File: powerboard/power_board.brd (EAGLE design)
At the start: 152.4 x 86.4 mm, 100 parts, among them Q1 IPP80P03P4L04AKSA1, U1 UWQ-12/20-T48NBS-C, U2 UWE-5/20-Q48NB-C, U3 UWE-3.3/30-Q48NB-C

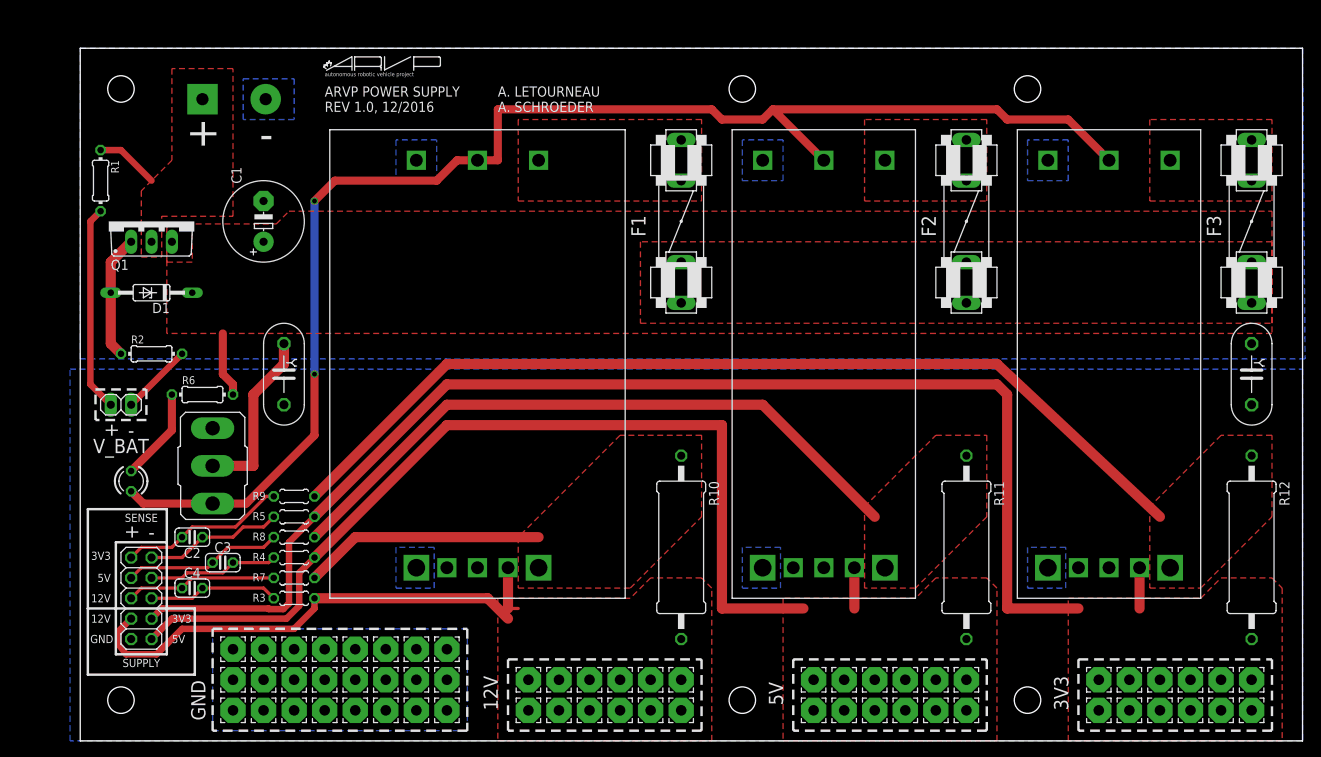
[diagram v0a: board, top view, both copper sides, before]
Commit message: Changed position of V_BAT current limiting resistor.
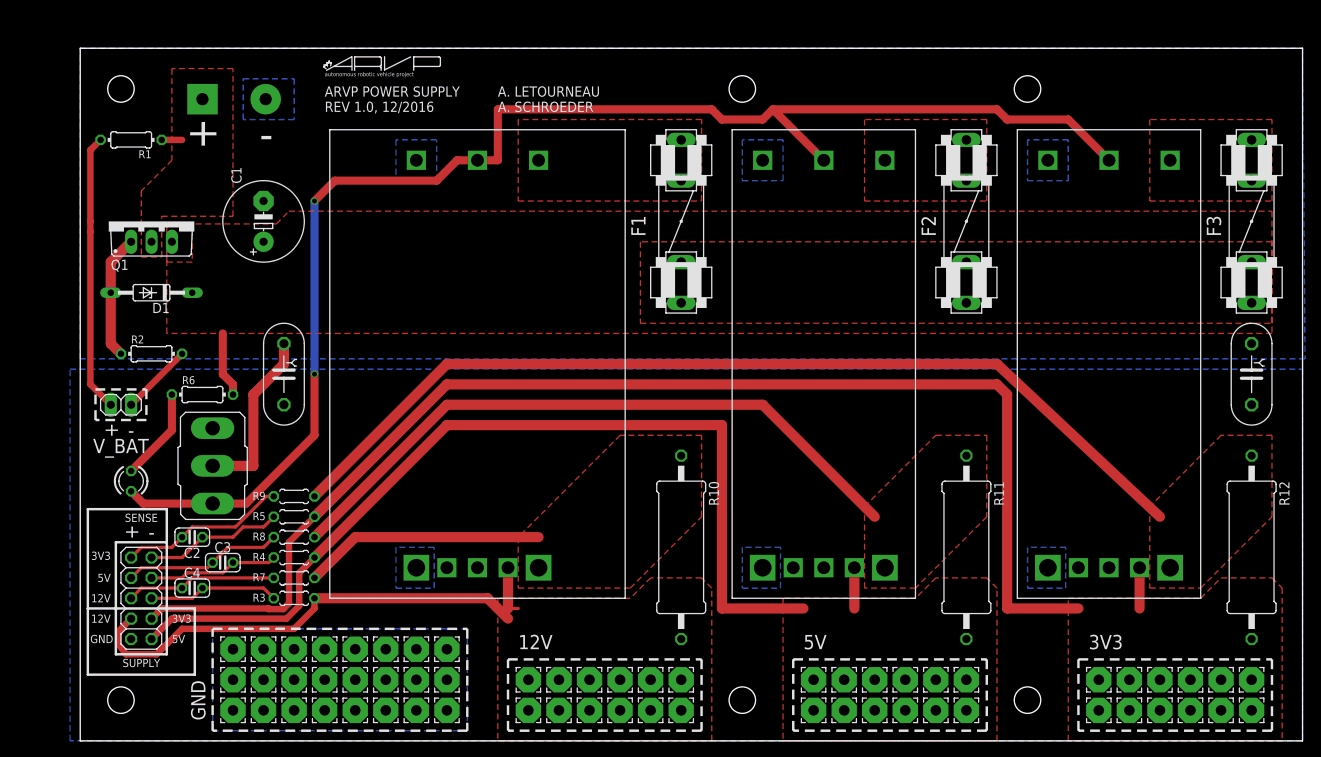
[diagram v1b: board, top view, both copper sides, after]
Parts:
- moved R1 6.35 mm to (35.6, 66.0), turned to 180 degrees
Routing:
- net N$2: track 25.7 -> 34.6 mm
- net VBAT+: track 7.93 -> 2.54 mm
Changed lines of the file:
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@@
 <setting verticaltext="up"/>
 </settings>
-<grid distance="1" unitdist="mm" unit="mm" style="lines" multiple="1" display="yes" altdistance="1" altunitdist="mm" altunit="mm"/>
+<grid distance="0.05" unitdist="inch" unit="inch" style="lines" multiple="1" display="yes" altdistance="0.0125" altunitdist="inch" altunit="inch"/>
 <layers>
 <layer number="1" name="Top" color="4" fill="1" visible="yes" active="yes"/>
@@
 <wire x1="106.68" y1="1.27" x2="106.68" y2="-7.62" width="0.3048" layer="25" style="longdash"/>
 <wire x1="106.68" y1="-7.62" x2="82.55" y2="-7.62" width="0.3048" layer="25" style="longdash"/>
-<text x="81.28" y="-5.08" size="1.778" layer="25" rot="R90">12V</text>
-<text x="116.84" y="-4.445" size="1.778" layer="25" rot="R90">5V</text>
-<text x="152.4" y="-5.08" size="1.778" layer="25" rot="R90">3V3</text>
+<text x="83.82" y="2.54" size="1.778" layer="25">12V</text>
+<text x="119.38" y="2.54" size="1.778" layer="25">5V</text>
+<text x="154.94" y="2.54" size="1.778" layer="25">3V3</text>
 <wire x1="118.11" y1="-7.62" x2="118.11" y2="1.27" width="0.3048" layer="25" style="longdash"/>
 <wire x1="118.11" y1="1.27" x2="142.24" y2="1.27" width="0.3048" layer="25" style="longdash"/>
@@
 </element>
 <element name="P$1" library="ARVP" package="AND_PWR" value="AND_PWR" x="44.45" y="71.12" rot="R90"/>
-<element name="R1" library="resistor" package="0204/7" value="1k" x="31.75" y="60.96" rot="R270"/>
+<element name="R1" library="resistor" package="0204/7" value="1k" x="35.56" y="66.04" rot="R180"/>
 </elements>
 <signals>
@@
 <contactref element="P$1" pad="PWR"/>
 <contactref element="R1" pad="1"/>
-<wire x1="31.75" y1="64.77" x2="34.29" y2="64.77" width="0.8128" layer="1"/>
-<wire x1="34.29" y1="64.77" x2="38.1" y2="60.96" width="0.8128" layer="1"/>
+<wire x1="39.37" y1="66.04" x2="41.91" y2="66.04" width="0.8128" layer="1"/>
 </signal>
 <signal name="N$4">
@@
 <contactref element="R1" pad="2"/>
 <contactref element="JP7" pad="1"/>
-<wire x1="31.75" y1="57.15" x2="30.48" y2="55.88" width="0.8128" layer="1"/>
-<wire x1="30.48" y1="55.88" x2="30.48" y2="35.56" width="0.8128" layer="1"/>
+<wire x1="30.48" y1="55.88" x2="30.48" y2="54.61" width="0.8128" layer="1"/>
+<wire x1="30.48" y1="54.61" x2="30.48" y2="35.56" width="0.8128" layer="1"/>
 <wire x1="30.48" y1="35.56" x2="33.02" y2="33.02" width="0.8128" layer="1"/>
+<wire x1="31.75" y1="66.04" x2="30.48" y2="64.77" width="0.8128" layer="1"/>
+<wire x1="30.48" y1="64.77" x2="30.48" y2="55.88" width="0.8128" layer="1"/>
 </signal>
 </signals>

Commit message: Removed toggle switch and added 2 position screw type terminal block.
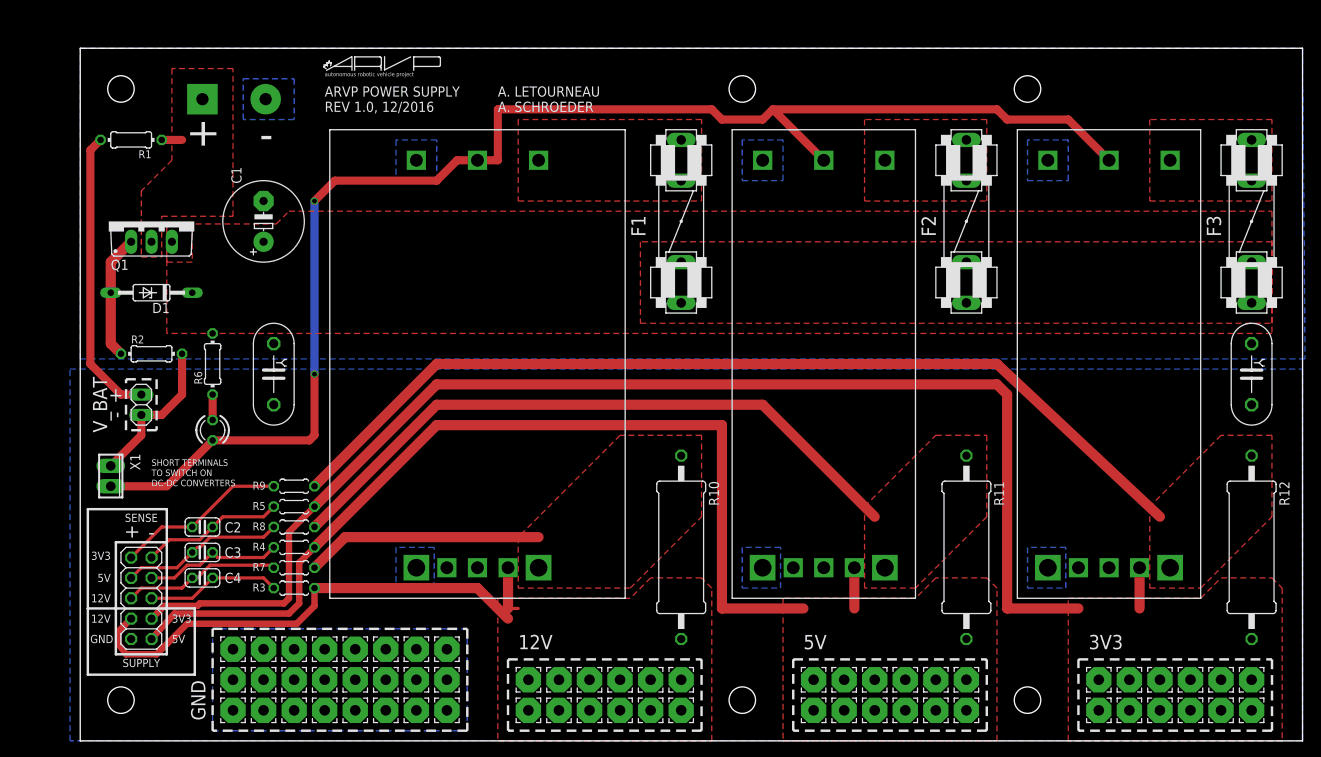
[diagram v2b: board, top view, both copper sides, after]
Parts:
- removed S1: (no value), switch:M9040P
- added X1: (no value), con-phoenix-254:2POL254
- moved LED1 12.0 mm to (45.7, 29.8)
- moved R6 4.02 mm to (45.7, 38.1), turned to 90 degrees
- moved C3 2.84 mm to (44.5, 14.6)
- moved JP7 2.54 mm to (36.8, 33.0), turned to 270 degrees
- moved C2 1.80 mm to (44.5, 17.8)
- moved C4 1.80 mm to (44.5, 11.4)
- moved R3 1.27 mm to (55.9, 10.2)
- moved R4 1.27 mm to (55.9, 15.2)
- moved R5 1.27 mm to (55.9, 20.3)
- moved R7 1.27 mm to (55.9, 12.7)
- moved R8 1.27 mm to (55.9, 17.8)
- moved R9 1.27 mm to (55.9, 22.9)
- moved CY1 1.27 mm to (53.3, 36.8)
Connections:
- net ON/OFF: now also X1.2; no longer S1.1
- net V-: now also X1.1; no longer S1.2
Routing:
- net V-: track 30.9 -> 19.1 mm
- net N$1: track 11.6 -> 3.18 mm
- net V+: track 8.15 -> 0.00 mm
- net N$2: track 34.6 -> 36.4 mm
- net 12V-SENSE: track 64.1 -> 65.7 mm
- net J5: track 16.3 -> 17.3 mm
- net ON/OFF: track 176.4 -> 177.4 mm
- net J4: track 18.8 -> 19.6 mm
- net 5V-SENSE: track 122.7 -> 123.3 mm
- net J8: track 20.9 -> 21.5 mm
- net J7: track 17.3 -> 17.9 mm
- net J3: track 16.3 -> 16.8 mm
- net 12V+SENSE: track 30.0 -> 29.5 mm
- net J6: track 19.9 -> 20.4 mm
- net 5V+SENSE: track 82.5 -> 81.9 mm
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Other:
- board text added: "DC-DC CONVERTERS"
- board text added: "SHORT TERMINALS"
- board text added: "TO SWITCH ON"

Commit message: Reduced length of board to 5.9 inches
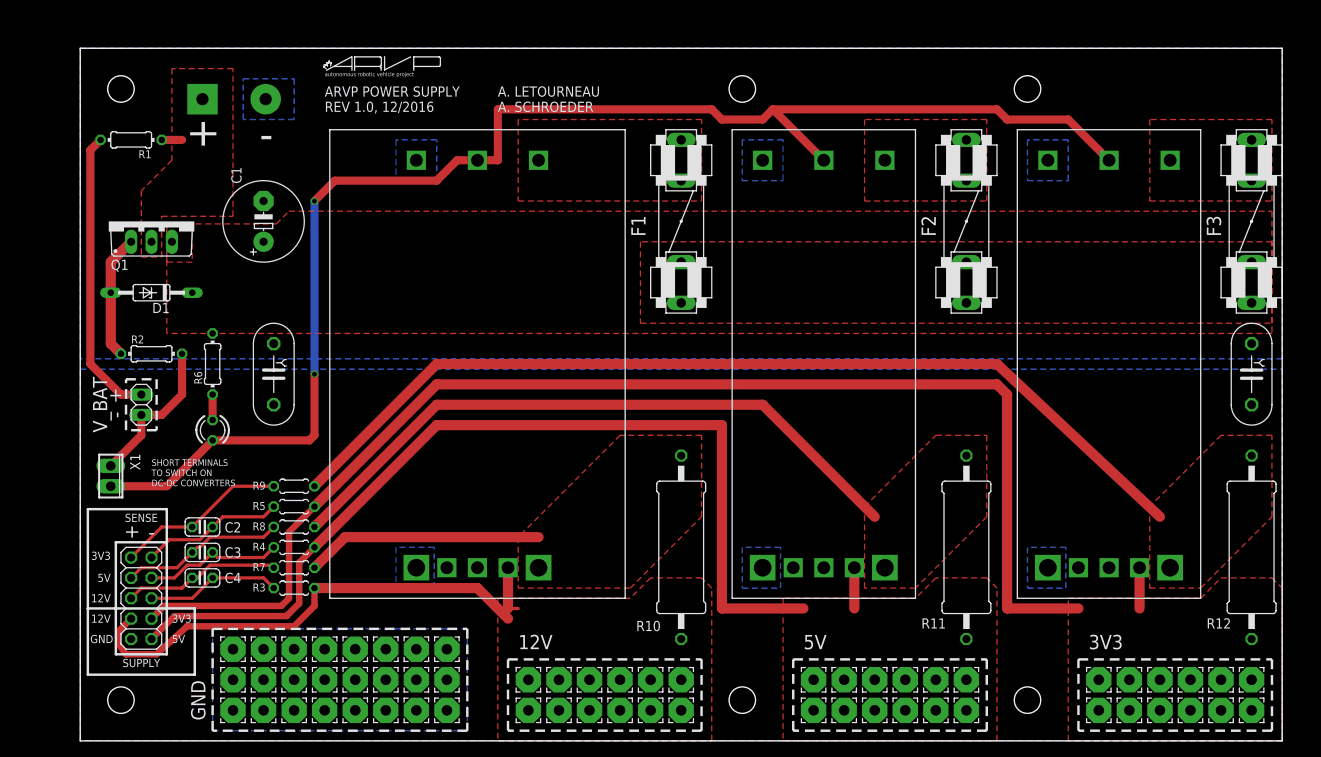
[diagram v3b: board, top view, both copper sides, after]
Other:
- board size 152.4 x 86.4 mm -> 149.9 x 86.4 mm
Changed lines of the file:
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@@
 <board>
 <plain>
-<wire x1="29.21" y1="-8.89" x2="181.61" y2="-8.89" width="0" layer="20"/>
-<wire x1="181.61" y1="-8.89" x2="181.61" y2="77.47" width="0" layer="20"/>
-<wire x1="181.61" y1="77.47" x2="29.21" y2="77.47" width="0" layer="20"/>
+<wire x1="29.21" y1="-8.89" x2="179.07" y2="-8.89" width="0" layer="20"/>
+<wire x1="179.07" y1="-8.89" x2="179.07" y2="77.47" width="0" layer="20"/>
+<wire x1="179.07" y1="77.47" x2="29.21" y2="77.47" width="0" layer="20"/>
 <wire x1="29.21" y1="77.47" x2="29.21" y2="-8.89" width="0" layer="20"/>
-<dimension x1="181.61" y1="-8.89" x2="181.61" y2="77.47" x3="193.04" y3="34.29" textsize="1.778" layer="20" unit="inch" precision="3" visible="yes"/>
-<dimension x1="181.61" y1="77.47" x2="29.21" y2="77.47" x3="105.41" y3="90.17" textsize="1.778" layer="20" unit="inch" precision="3" visible="yes"/>
+<dimension x1="179.07" y1="-8.89" x2="179.07" y2="77.47" x3="190.5" y3="34.29" textsize="1.778" layer="20" unit="inch" precision="3" visible="yes"/>
 <text x="33.02" y="6.35" size="1.016" layer="25" align="center-right">12V</text>
 <text x="40.64" y="3.81" size="1.016" layer="25" align="center-left">5V</text>
@@
 <text x="38.1" y="24.13" size="0.8128" layer="25">TO SWITCH ON</text>
 <text x="38.1" y="22.86" size="0.8128" layer="25">DC-DC CONVERTERS</text>
+<dimension x1="179.07" y1="77.47" x2="29.21" y2="77.47" x3="104.14" y3="91.44" textsize="1.778" layer="20" unit="inch" visible="yes"/>
 </plain>
 <attributes>
@@
 <attribute name="VALUE" x="171.069" y="40.767" size="1.27" layer="27" ratio="10" rot="R270"/>
 </element>
-<element name="R10" library="rcl" package="0617/22" value="0.004" x="104.14" y="15.24" rot="R270"/>
-<element name="R11" library="rcl" package="0617/22" value="0.004" x="139.7" y="15.24" rot="R270"/>
-<element name="R12" library="rcl" package="0617/22" value="0.004" x="175.26" y="15.24" rot="R270"/>
+<element name="R10" library="rcl" package="0617/22" value="0.004" x="104.14" y="15.24" smashed="yes" rot="R270">
+<attribute name="NAME" x="101.6" y="6.0706" size="1.27" layer="25" ratio="10" rot="R180"/>
+<attribute name="VALUE" x="103.5558" y="21.717" size="1.27" layer="27" ratio="10" rot="R270"/>
+</element>
+<element name="R11" library="rcl" package="0617/22" value="0.004" x="139.7" y="15.24" smashed="yes" rot="R270">
+<attribute name="NAME" x="137.16" y="6.3881" size="1.27" layer="25" ratio="10" rot="R180"/>
+<attribute name="VALUE" x="139.1158" y="21.717" size="1.27" layer="27" ratio="10" rot="R270"/>
+</element>
+<element name="R12" library="rcl" package="0617/22" value="0.004" x="175.26" y="15.24" smashed="yes" rot="R270">
+<attribute name="NAME" x="172.72" y="6.3881" size="1.27" layer="25" ratio="10" rot="R180"/>
+<attribute name="VALUE" x="174.6758" y="21.717" size="1.27" layer="27" ratio="10" rot="R270"/>
+</element>
 <element name="JP8" library="pinhead" package="2X05" value="" x="36.83" y="8.89" smashed="yes" rot="R90">
 <attribute name="VALUE" x="41.275" y="2.54" size="1.27" layer="27" rot="R90"/>
@@
 <polygon width="0.3048" layer="16">
 <vertex x="29.21" y="77.47"/>
-<vertex x="181.61" y="77.47"/>
-<vertex x="181.9275" y="38.735"/>
+<vertex x="179.07" y="77.47"/>
+<vertex x="179.07" y="38.735"/>
 <vertex x="29.21" y="38.735"/>
 </polygon>
@@
 <signal name="GND">
 <polygon width="0.3048" layer="16">
-<vertex x="181.61" y="37.465"/>
-<vertex x="181.61" y="-8.89"/>
-<vertex x="27.94" y="-8.89"/>
-<vertex x="27.94" y="37.465"/>
+<vertex x="179.07" y="37.465"/>
+<vertex x="179.07" y="-8.89"/>
+<vertex x="29.21" y="-8.89"/>
+<vertex x="29.21" y="37.465"/>
 </polygon>
 <contactref element="U1" pad="-VOUT"/>
@@
 <contactref element="JP8" pad="4"/>
 <wire x1="58.42" y1="10.16" x2="58.42" y2="7.9375" width="0.8128" layer="1"/>
-<wire x1="58.42" y1="7.9375" x2="56.1975" y2="5.715" width="0.8128" layer="1"/>
-<wire x1="56.1975" y1="5.715" x2="42.545" y2="5.715" width="0.8128" layer="1"/>
-<wire x1="42.545" y1="5.715" x2="38.735" y2="1.905" width="0.8128" layer="1"/>
+<wire x1="58.42" y1="7.9375" x2="55.88" y2="5.3975" width="0.8128" layer="1"/>
+<wire x1="55.88" y1="5.3975" x2="42.545" y2="5.3975" width="0.8128" layer="1"/>
+<wire x1="42.545" y1="5.3975" x2="38.735" y2="1.905" width="0.8128" layer="1"/>
 <wire x1="38.735" y1="1.905" x2="34.925" y2="1.905" width="0.8128" layer="1"/>
 <wire x1="34.925" y1="1.905" x2="33.9725" y2="3.175" width="0.8128" layer="1"/>
@@
 <wire x1="58.42" y1="15.24" x2="56.515" y2="13.335" width="0.8128" layer="1"/>
 <wire x1="56.515" y1="13.335" x2="56.515" y2="8.255" width="0.8128" layer="1"/>
-<wire x1="56.515" y1="8.255" x2="55.245" y2="6.985" width="0.8128" layer="1"/>
-<wire x1="55.245" y1="6.985" x2="40.9575" y2="6.985" width="0.8128" layer="1"/>
-<wire x1="40.9575" y1="6.985" x2="38.1" y2="3.81" width="0.8128" layer="1"/>
+<wire x1="56.515" y1="8.255" x2="54.9275" y2="6.6675" width="0.8128" layer="1"/>
+<wire x1="54.9275" y1="6.6675" x2="40.9575" y2="6.6675" width="0.8128" layer="1"/>
+<wire x1="40.9575" y1="6.6675" x2="38.1" y2="3.81" width="0.8128" layer="1"/>
 </signal>
 <signal name="3V3-SENSE">
@@
 <wire x1="55.245" y1="17.145" x2="55.245" y2="8.89" width="0.8128" layer="1"/>
 <wire x1="39.6875" y1="7.9375" x2="38.1" y2="6.35" width="0.8128" layer="1"/>
-<wire x1="55.245" y1="8.89" x2="54.61" y2="8.255" width="0.8128" layer="1"/>
-<wire x1="54.61" y1="8.255" x2="44.1325" y2="8.255" width="0.8128" layer="1"/>
-<wire x1="44.1325" y1="8.255" x2="43.815" y2="7.9375" width="0.8128" layer="1"/>
-<wire x1="43.815" y1="7.9375" x2="39.6875" y2="7.9375" width="0.8128" layer="1"/>
+<wire x1="55.245" y1="8.89" x2="54.2925" y2="7.9375" width="0.8128" layer="1"/>
+<wire x1="54.2925" y1="7.9375" x2="39.6875" y2="7.9375" width="0.8128" layer="1"/>
 </signal>
 <signal name="N$1">

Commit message: Modified PCB Layout, doubled number of supply pin headers
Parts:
- JP8: device pinhead:2X05 -> pinhead:2X07
- moved X1 21.6 mm to (33.0, 2.54)
- moved JP8 8.89 mm to (36.8, 17.8)
- moved C3 7.73 mm to (45.7, 22.2), turned to 0 degrees
- moved C4 7.73 mm to (45.7, 19.1), turned to 0 degrees
- moved C2 7.73 mm to (45.7, 25.4), turned to 0 degrees
- moved R4 2.54 mm to (55.9, 17.8)
- moved R7 2.54 mm to (55.9, 15.2)
- moved R3 2.54 mm to (55.9, 12.7)
- moved R5 2.54 mm to (55.9, 22.9)
- moved R8 2.54 mm to (55.9, 20.3)
- moved R9 2.54 mm to (55.9, 25.4)
- moved CY1 0.32 mm to (53.3, 36.5)
- moved CY2 0.32 mm to (175.3, 36.5)
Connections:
- net 12V-SENSE: now also JP8.1, JP8.2; no longer JP8.4
- net 3V3-SENSE: now also JP8.5, JP8.6; no longer JP8.3
- net 5V-SENSE: now also JP8.3, JP8.4; no longer JP8.1
- net GND: now also JP8.7, JP8.8; no longer JP8.2
- net J3: now also JP8.9; no longer JP8.5
- net J4: now also JP8.10; no longer JP8.6
- net J5: now also JP8.11; no longer JP8.7
- net J6: now also JP8.12; no longer JP8.8
- net J7: now also JP8.13; no longer JP8.9
- net J8: now also JP8.14; no longer JP8.10
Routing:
- net ON/OFF: track 177.4 -> 204.8 mm
- net V-: track 19.1 -> 45.8 mm
- net 12V-SENSE: track 65.6 -> 59.0 mm
- net J8: track 21.5 -> 18.8 mm
- net J3: track 16.8 -> 18.4 mm
- net J7: track 17.9 -> 16.3 mm
- net J4: track 19.6 -> 20.9 mm
- net 12V+SENSE: track 29.5 -> 28.5 mm
- net 3V3-SENSE: track 164.8 -> 165.7 mm
- net 5V-SENSE: track 123.2 -> 123.8 mm
- net J6: track 20.4 -> 19.9 mm
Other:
- board text added: "REV 1.0, 02/2017"
- board text added: "USE SOLDER FLUX WHEN SOLDERING INTO WIRE PADS!"
- board text removed: "REV 1.0, 12/2016"
